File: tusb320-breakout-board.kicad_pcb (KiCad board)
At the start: 2 copper layers, 11.4 x 32.5 mm, 7 parts, among them J1 USB-C Receptacle (USB 2.0), J2 Left Header Pins, J3 Right Header Pins, U1 TUSB320

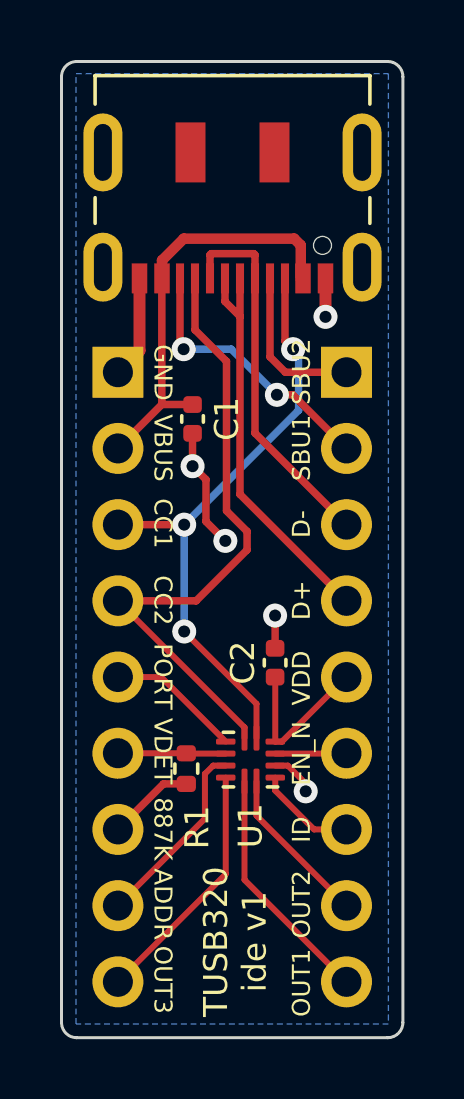
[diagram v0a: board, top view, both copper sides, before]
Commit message: Add jumper to connect VBUS to VBUS_DET
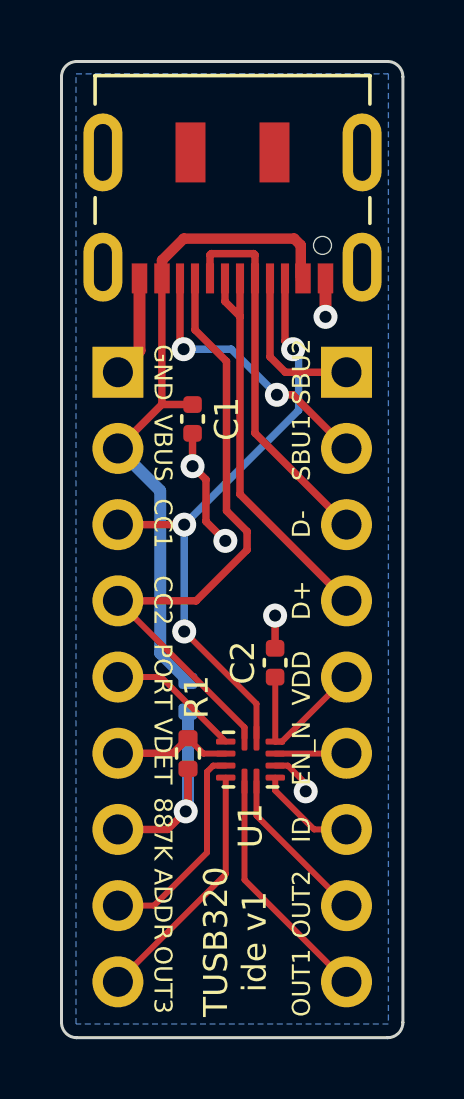
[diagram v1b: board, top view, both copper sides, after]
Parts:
- added R2: 0K, Resistor_SMD:R_0402_1005Metric, B.Cu at (121.1, 92.8)
- moved R1 0.51 mm to (121.1, 94.7)
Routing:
- net Net-(C1-Pad2): track 14.0 -> 22.7 mm
- net Net-(J2-Pad7): track 2.91 -> 7.32 mm, vias 0 -> 1
- net Net-(J2-Pad8): track 6.40 -> 7.11 mm
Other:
- board text added: "Bridge to connect VBUS and VBUS_DET"
